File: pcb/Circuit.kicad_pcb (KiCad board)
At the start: 2 copper layers, 82.4 x 68.9 mm, 48 parts, among them J1 DTM13-12PA-R008, J2 TSW-101-07-T-D, J3 TSW-101-07-T-D, U1 MCP1700-1802E_TO92, U2 CDP68HC68S1, U3 LM2672N-5.0, U4 Teensy4.0, U5 MCP2562-H-P

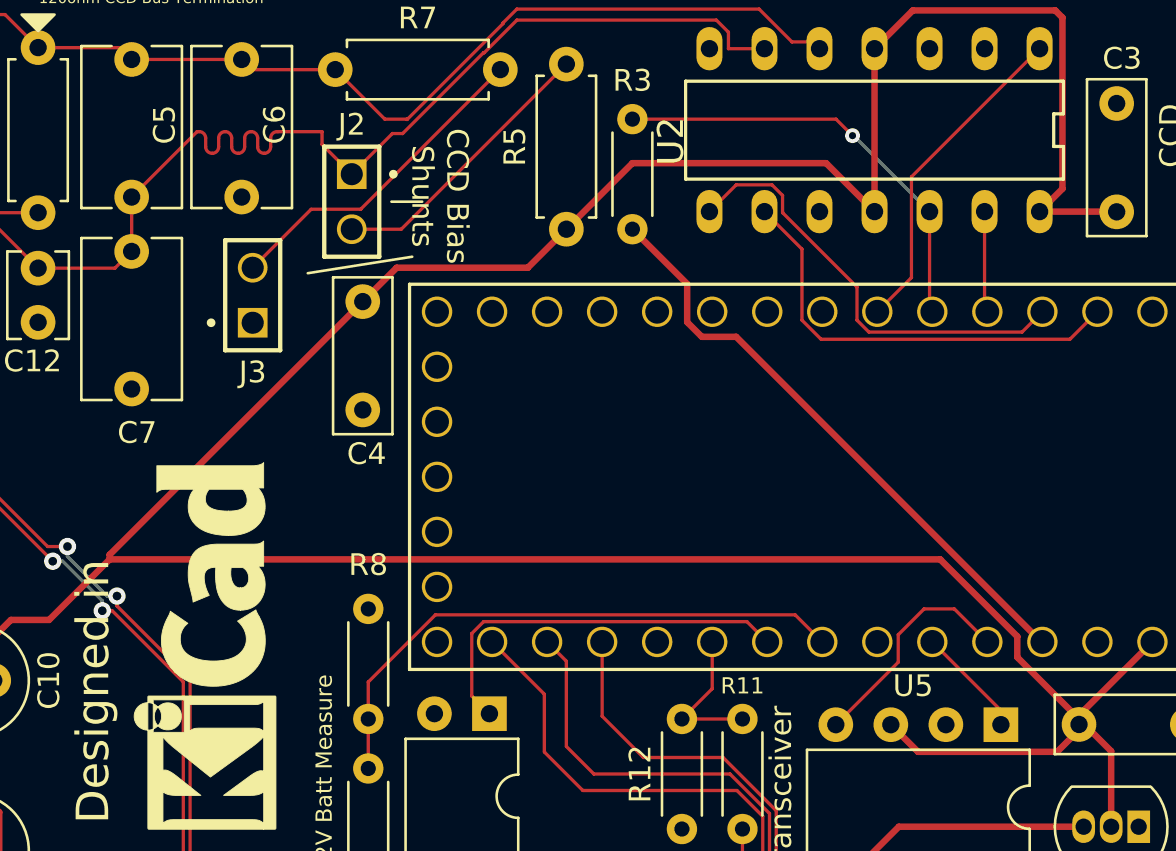
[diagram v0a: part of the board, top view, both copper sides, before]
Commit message: Move speedo to a FlexPWM pin
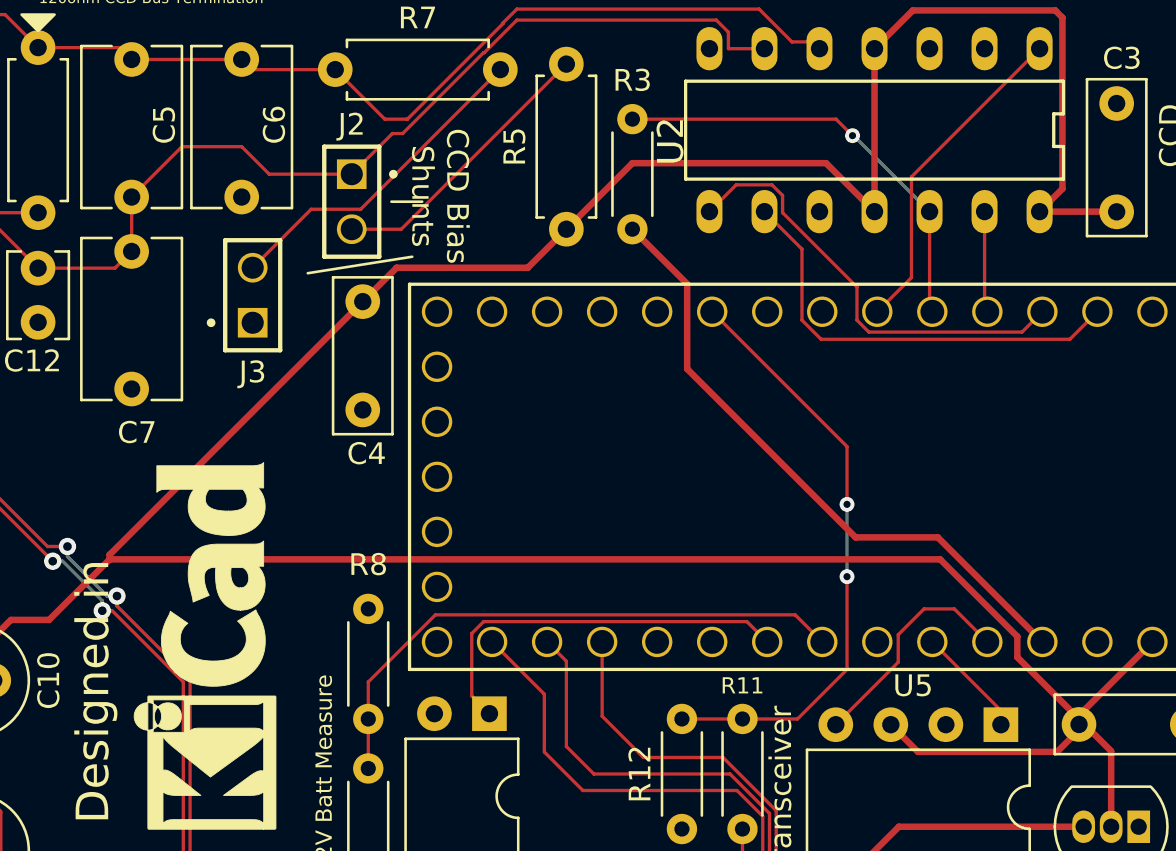
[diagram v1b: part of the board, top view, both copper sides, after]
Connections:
- U4 pad 25: SPEEDO -> unconnected-(U4-Pad25)
- U4 pad 9: unconnected-(U4-Pad9) -> SPEEDO
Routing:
- net SPEEDO: track 6.93 -> 28.0 mm, vias 0 -> 2
- net ccd_f-: track 59.8 -> 54.6 mm
- net 3v3: track 27.8 -> 29.1 mm

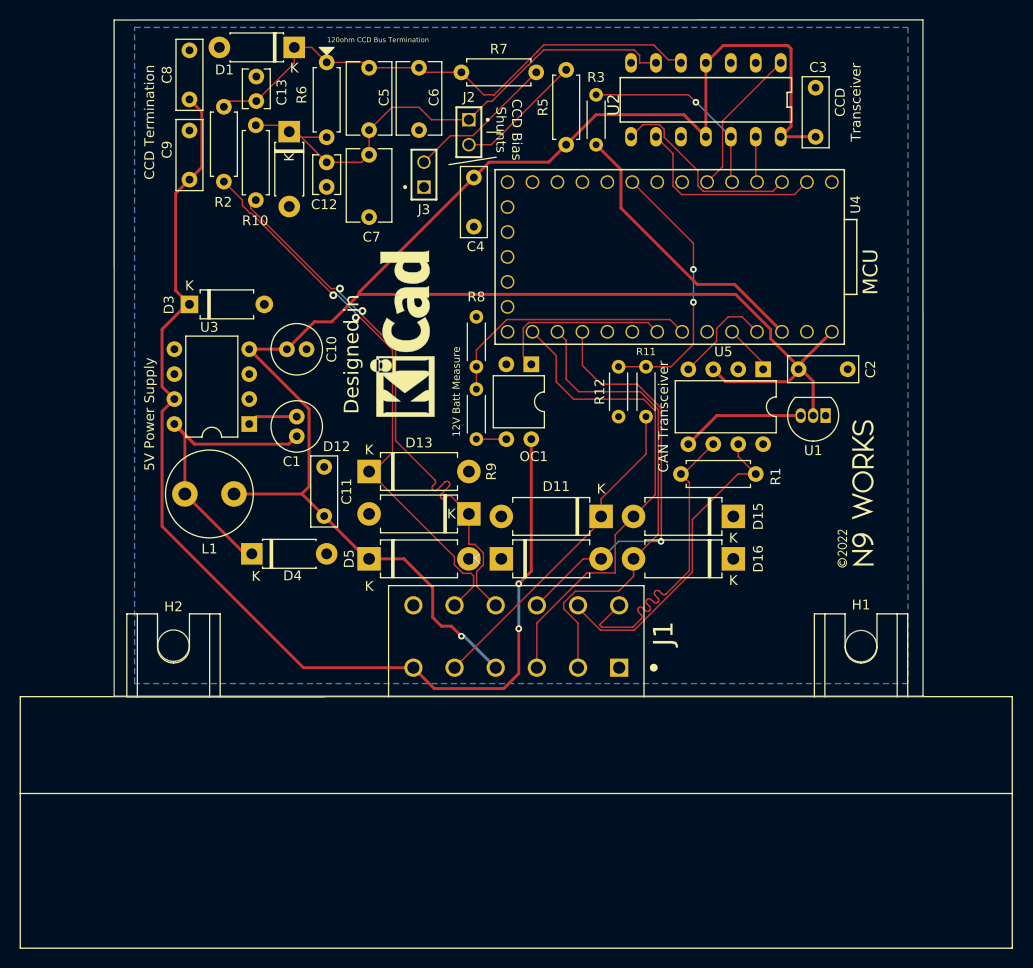
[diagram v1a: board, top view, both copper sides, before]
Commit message: Update for actual parts ordered from Mouser
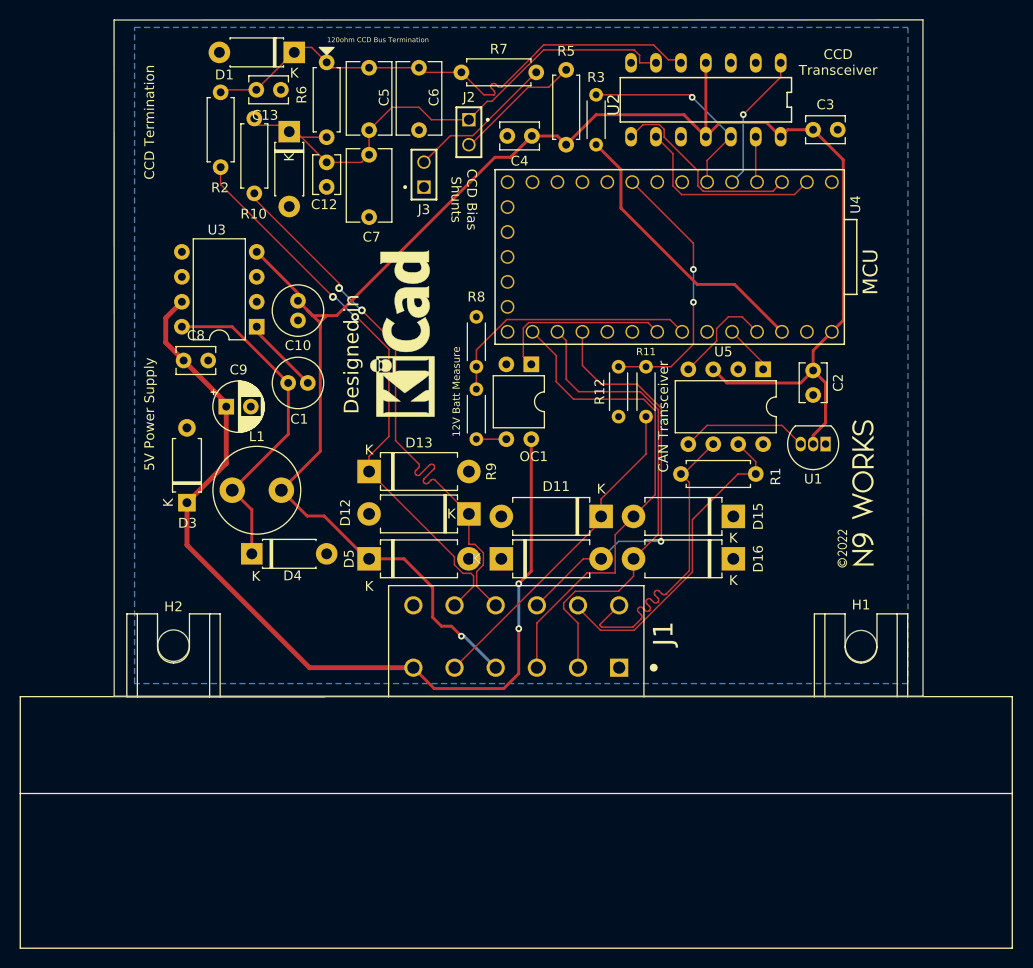
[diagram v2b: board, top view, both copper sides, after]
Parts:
- removed C11: 0.1uf, Capacitor_THT:C_Disc_D7.0mm_W2.5mm_P5.00mm
- C2, C3, C4, C8: footprint Capacitor_THT:C_Disc_D7.0mm_W2.5mm_P5.00mm -> Capacitor_THT:C_Disc_D3.8mm_W2.6mm_P2.50mm
- C9: footprint Capacitor_THT:C_Disc_D7.0mm_W2.5mm_P5.00mm -> Capacitor_THT:CP_Radial_D5.0mm_P2.50mm
- moved C8 26.6 mm to (57.3, 101.2), turned to 0 degrees
- moved C9 23.4 mm to (61.7, 105.9), turned to 0 degrees
- moved D3 20.2 mm to (57.7, 115.7), turned to 90 degrees
- moved U3 9.94 mm to (64.8, 97.8)
- moved C4 7.26 mm to (92.8, 78.4), turned to 180 degrees
- moved C10 5.06 mm to (69.0, 95.1), turned to -90 degrees
- moved L1 4.84 mm to (62.3, 114.4)
- moved C1 3.61 mm to (70.0, 103.5), turned to 180 degrees
- moved U1 2.90 mm to (122.7, 109.7)
- moved R2 1.51 mm to (61.1, 81.5)
- moved C2 1.49 mm to (121.4, 102.2), turned to -90 degrees
- moved C13 1.15 mm to (64.7, 73.7), turned to 0 degrees
- moved C3 0.77 mm to (121.4, 77.7), turned to 0 degrees
- moved R10 0.70 mm to (64.5, 84.2)
- moved D1 0.51 mm to (68.6, 69.8)
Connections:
- U4 pad 5: idle -> CCD_CLOCK
- U4 pad 6: CCD_CLOCK -> idle
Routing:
- net +5V: track 209.8 -> 178.9 mm
- net +12V: track 116.2 -> 94.5 mm
- net Net-(C1-Pad1): track 5.15 -> 7.89 mm
- net Net-(C1-Pad2): track 32.5 -> 33.8 mm
- net CCD_CLOCK: track 15.2 -> 14.2 mm, vias 0 -> 1
- net idle: track 20.2 -> 21.2 mm
- net ccd+: track 57.8 -> 58.5 mm

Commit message: Circuit using LM2591HVT
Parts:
- removed C1: 10nF, Capacitor_THT:C_Radial_D5.0mm_H11.0mm_P2.00mm
- removed C8: 0.1uf, Capacitor_THT:C_Disc_D3.8mm_W2.6mm_P2.50mm
- C10: value 68uF -> 220uF
- C9: value 100uF -> 680uF
- D3: value SD15_SOD323 -> P6KE56CA; footprint Diode_THT:D_A-405_P7.62mm_Horizontal -> Diode_THT:D_DO-15_P10.16mm_Horizontal
- L1: value 47uH -> 33uH
- U3: value LM2672N-5.0 -> LM2591HVT-5.0; footprint Package_DIP:DIP-8_W7.62mm -> Power_Regulator:TO170P1016X470X2092-5
- moved D3 10.5 mm to (57.9, 105.2), turned to -90 degrees
- moved C9 2.16 mm to (63.8, 105.9)
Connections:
- D3 pad 1: +12V -> GND
- D3 pad 2: GND -> +12V
- D4 pad 1: Net-(C1-Pad2) -> Net-(D4-Pad1)
- L1 pad 1: Net-(C1-Pad2) -> Net-(D4-Pad1)
- U3 pad 1: Net-(C1-Pad1) -> +12V
- U3 pad 2: unconnected-(U3-Pad2) -> Net-(D4-Pad1)
- U3 pad 3: unconnected-(U3-Pad3) -> GND
- U3 pad 5: unconnected-(U3-Pad5) -> GND
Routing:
- net Net-(C1-Pad2): track 33.8 -> 0.00 mm
- net Net-(D4-Pad1): track 0.00 -> 32.2 mm
- net Net-(C1-Pad1): track 7.89 -> 0.00 mm
- net GND: track 0.00 -> 5.11 mm
- net +12V: track 94.5 -> 89.7 mm
- net +5V: track 178.9 -> 183.6 mm
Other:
- board text added: "Speed Sensor"
